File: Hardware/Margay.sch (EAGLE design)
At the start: 70 parts, among them IC1 ATMEGA644M, J1 CONN_42.54_SCREW, J2 CONN_6SCREW_2.54, Q1 FDN360P, Q2 DMG3404, Q3 2N7002, Q4 FDN360P, Q6 FDN360P, U2 FT231X-Q

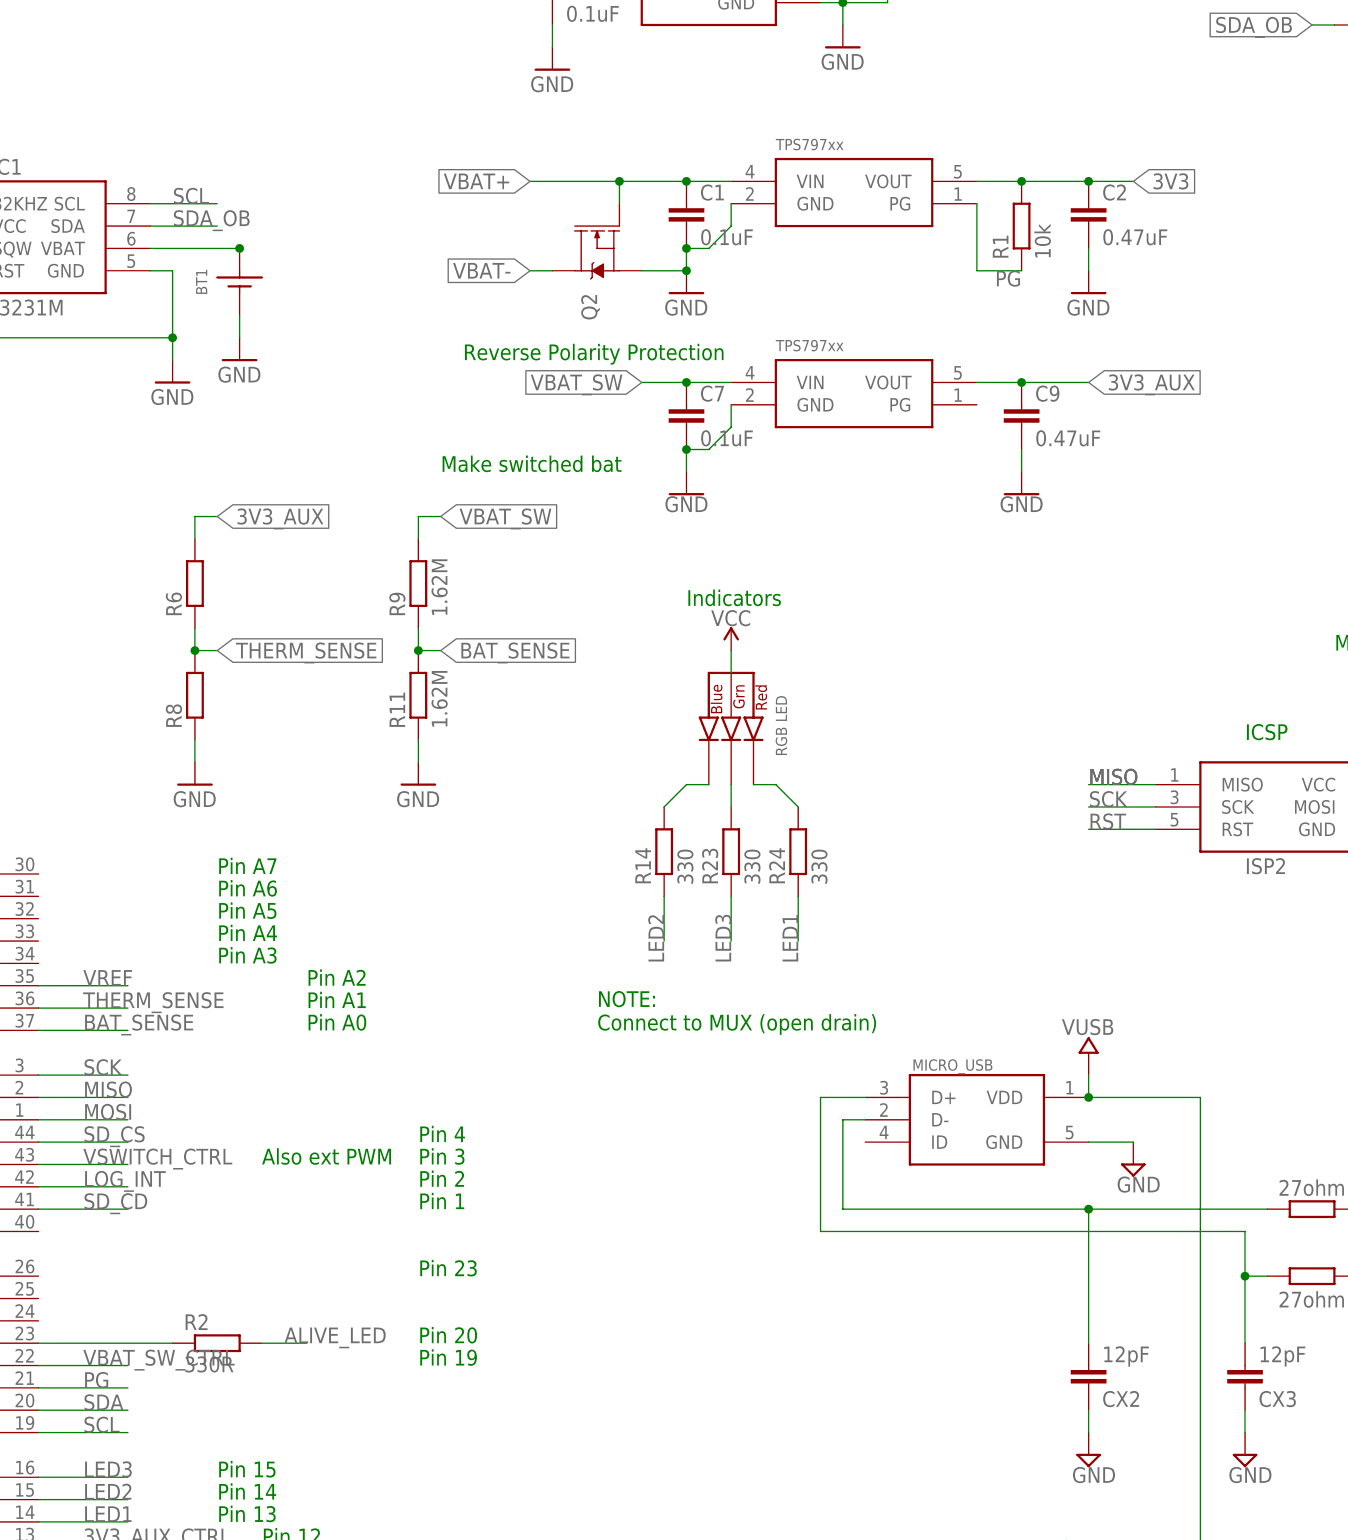
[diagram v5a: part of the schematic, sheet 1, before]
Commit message: Minor mod to hardware test, added BOM
Added independent BOM and did some clean up on the schematic
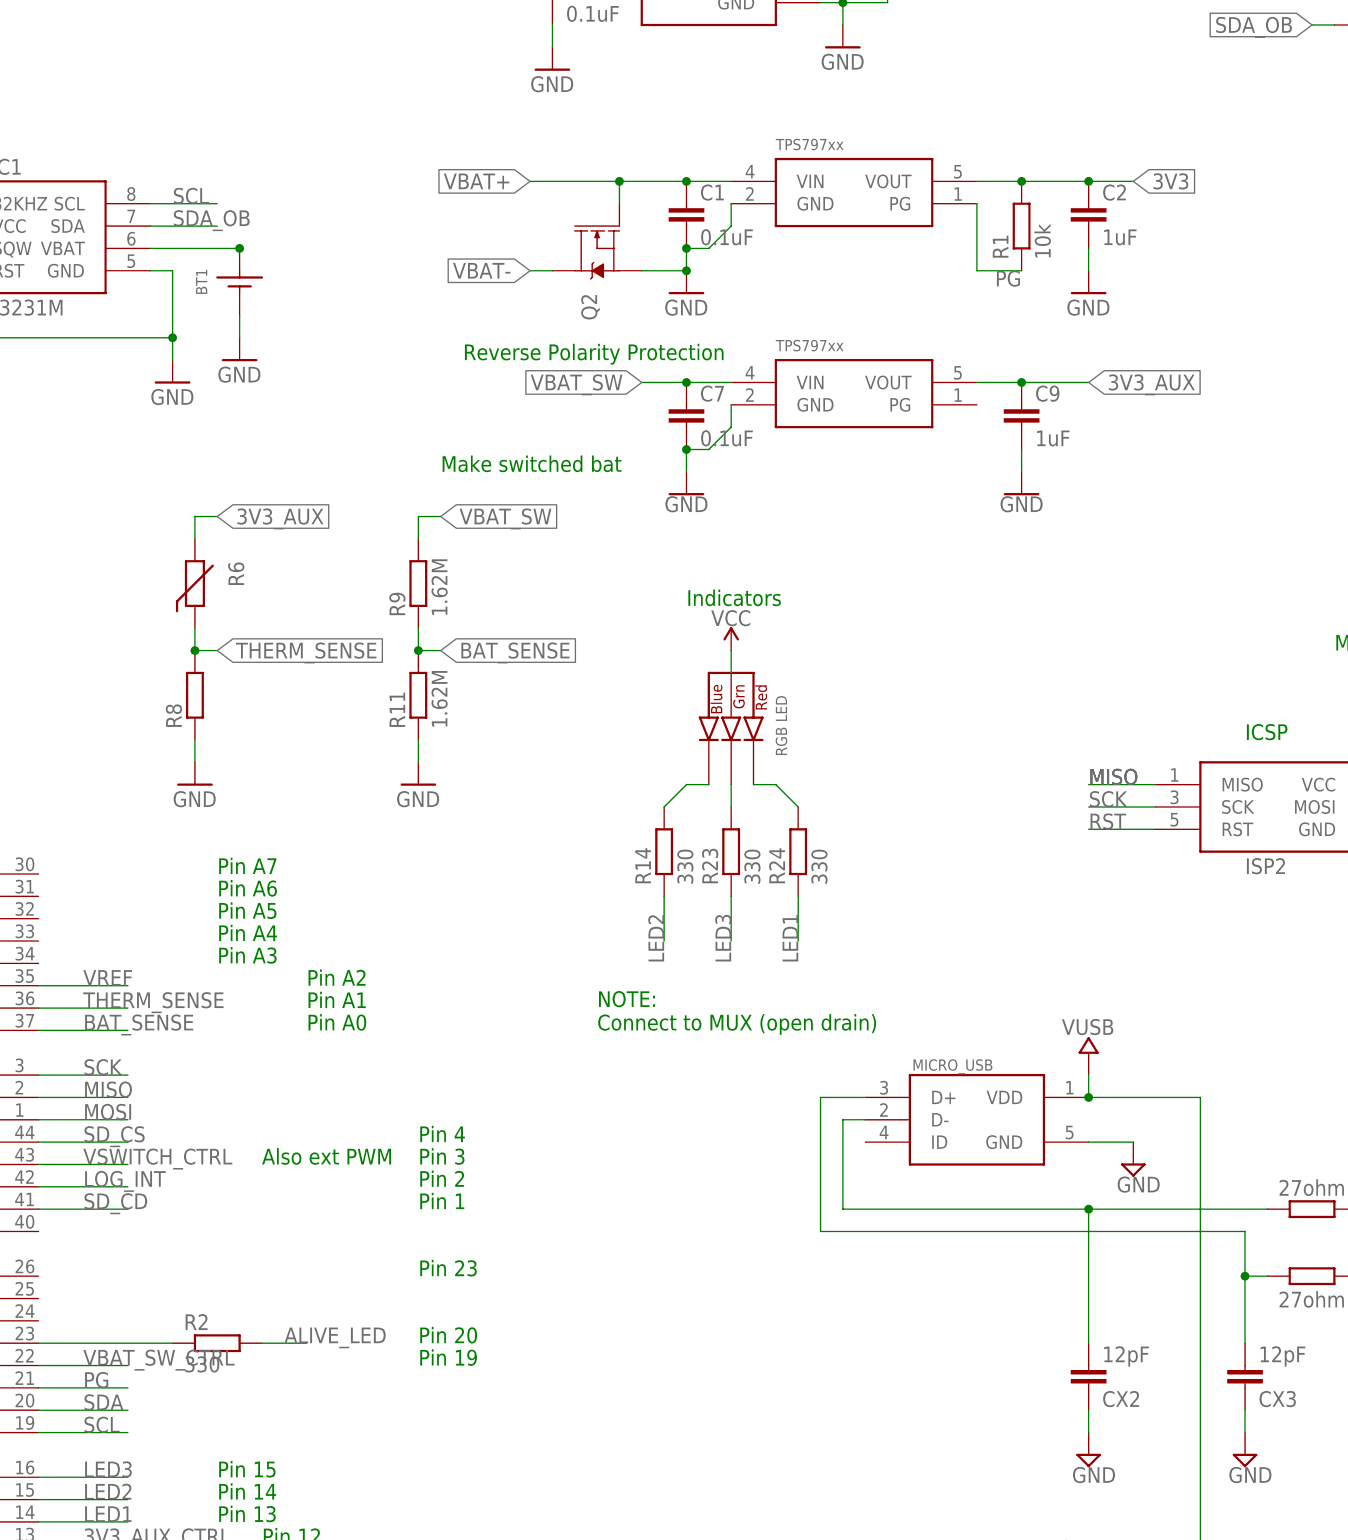
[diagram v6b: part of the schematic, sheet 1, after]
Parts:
- C1, C3, C4, C7: device bschulz_passives:C-EUC0603 -> bschulz_passives:C-EU0.1UFC0603
- C2, C9: value 0.47uF -> 1uF; device bschulz_passives:C-EUC0603 -> bschulz_passives:C-EU1UFC0603
- C25, C5: device bschulz:C-EU12PFC0603 -> bschulz_passives:C-EU12PFC0603
- C8: device bschulz:C-EUC0603 -> bschulz_passives:C-EU0.1UFC0603
- R1, R12, R15: device bschulz:R-EU_R0603 -> bschulz_passives:R-EU_10KR0603
- R11, R9: device bschulz:R-EU_R0603 -> bschulz_passives:R-EU_1.62MR0603
- R16: device bschulz_passives:R-EU_R0603 -> bschulz_passives:R-EU_180KR0603
- R17: device bschulz_passives:R-EU_R0603 -> bschulz_passives:R-EU_10KR0603
- R2: value 330R -> 330; device bschulz:R-EU_R0603 -> bschulz:R-EU_330R0603
- R6: device bschulz:R-EU_R0603 -> bschulz:THERMISTOR10K; DIGIKEY (none) -> 490-16279-1-ND; MF (none) -> Murata; MPN (none) -> NCU18XH103F60RB
- R8: DIGIKEY (none) -> P10KDBCT-ND; MF (none) -> Panasonic; MPN (none) -> ERA-3AEB103V
- U$3: device adafruit:SDMMC06132 -> bschulz:SDMMC06132
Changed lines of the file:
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@@
 <part name="U$9" library="bschulz" deviceset="BUTTON" device="4.2X3.2"/>
 <part name="GND20" library="SparkFun-PowerSymbols" deviceset="GND" device=""/>
-<part name="C25" library="bschulz" deviceset="C-EU" device="C0603" technology="12PF" value="12pF">
+<part name="C25" library="bschulz_passives" deviceset="C-EU" device="C0603" technology="12PF" value="12pF">
 <attribute name="DIGIKEY" value="1276-1254-1-ND"/>
 <attribute name="MF" value="Samsung"/>
@@
 </part>
 <part name="U$16" library="bschulz" deviceset="CLVBA-FKA" device=""/>
-<part name="C5" library="bschulz" deviceset="C-EU" device="C0603" technology="12PF" value="12pF">
+<part name="C5" library="bschulz_passives" deviceset="C-EU" device="C0603" technology="12PF" value="12pF">
 <attribute name="DIGIKEY" value="1276-1254-1-ND"/>
 <attribute name="MF" value="Samsung"/>
@@
 </part>
 <part name="C6" library="bschulz" deviceset="C-EU" device="C0603" technology="0.1UF" value="0.1uF"/>
-<part name="C8" library="bschulz" deviceset="C-EU" device="C0603" value="0.1uF"/>
+<part name="C8" library="bschulz_passives" deviceset="C-EU" device="C0603" technology="0.1UF" value="0.1uF"/>
 <part name="U$20" library="MyPOW" deviceset="VUSB" device=""/>
-<part name="U$3" library="adafruit" library_urn="urn:adsk.eagle:library:420" deviceset="SDMMC" device="06132"/>
+<part name="U$3" library="bschulz" deviceset="SDMMC" device="06132"/>
 <part name="Q1" library="bschulz" deviceset="MOSFET_PCH" device="-FDN360P" value="FDN360P"/>
 <part name="U$4" library="bschulz" deviceset="MIC842" device="" technology="H" value="MIC842H"/>
@@
 <part name="JP1" library="SparkFun-Jumpers" library_urn="urn:adsk.eagle:library:528" deviceset="JUMPER-SMT_3_1-NC_PASTE" device="_SILK" package3d_urn="urn:adsk.eagle:package:39293/1"/>
 <part name="U$6" library="bschulz" deviceset="TPS797*" device="" technology="33"/>
-<part name="C1" library="bschulz_passives" deviceset="C-EU" device="C0603" value="0.1uF"/>
+<part name="C1" library="bschulz_passives" deviceset="C-EU" device="C0603" technology="0.1UF" value="0.1uF"/>
 <part name="GND2" library="supply1" library_urn="urn:adsk.eagle:library:371" deviceset="GND" device=""/>
-<part name="C2" library="bschulz_passives" deviceset="C-EU" device="C0603" value="0.47uF"/>
+<part name="C2" library="bschulz_passives" deviceset="C-EU" device="C0603" technology="1UF" value="1uF"/>
 <part name="GND3" library="supply1" library_urn="urn:adsk.eagle:library:371" deviceset="GND" device=""/>
-<part name="R1" library="bschulz" deviceset="R-EU_" device="R0603" value="10k"/>
-<part name="R2" library="bschulz" deviceset="R-EU_" device="R0603" value="330R"/>
-<part name="R6" library="bschulz" deviceset="R-EU_" device="R0603"/>
-<part name="R8" library="bschulz" deviceset="R-EU_" device="R0603"/>
-<part name="R9" library="bschulz" deviceset="R-EU_" device="R0603" value="1.62M"/>
-<part name="R11" library="bschulz" deviceset="R-EU_" device="R0603" value="1.62M"/>
+<part name="R1" library="bschulz_passives" deviceset="R-EU_" device="R0603" technology="10K" value="10k"/>
+<part name="R2" library="bschulz" deviceset="R-EU_" device="R0603" technology="330" value="330"/>
+<part name="R6" library="bschulz" deviceset="THERMISTOR" device="" technology="10K">
+<attribute name="DIGIKEY" value="490-16279-1-ND"/>
+<attribute name="MF" value="Murata"/>
+<attribute name="MPN" value="NCU18XH103F60RB"/>
+</part>
+<part name="R8" library="bschulz" deviceset="R-EU_" device="R0603">
+<attribute name="DIGIKEY" value="P10KDBCT-ND "/>
+<attribute name="MF" value="Panasonic"/>
+<attribute name="MPN" value="ERA-3AEB103V"/>
+</part>
+<part name="R9" library="bschulz_passives" deviceset="R-EU_" device="R0603" technology="1.62M" value="1.62M"/>
+<part name="R11" library="bschulz_passives" deviceset="R-EU_" device="R0603" technology="1.62M" value="1.62M"/>
 <part name="GND4" library="supply1" library_urn="urn:adsk.eagle:library:371" deviceset="GND" device=""/>
 <part name="GND5" library="supply1" library_urn="urn:adsk.eagle:library:371" deviceset="GND" device=""/>
 <part name="U$7" library="bschulz" deviceset="MAX6070AAUT*" device="" technology="18"/>
-<part name="C3" library="bschulz_passives" deviceset="C-EU" device="C0603" value="0.1uF"/>
-<part name="C4" library="bschulz_passives" deviceset="C-EU" device="C0603" value="0.1uF"/>
+<part name="C3" library="bschulz_passives" deviceset="C-EU" device="C0603" technology="0.1UF" value="0.1uF"/>
+<part name="C4" library="bschulz_passives" deviceset="C-EU" device="C0603" technology="0.1UF" value="0.1uF"/>
 <part name="GND6" library="supply1" library_urn="urn:adsk.eagle:library:371" deviceset="GND" device=""/>
 <part name="U$8" library="bschulz" deviceset="MCP3425" device=""/>
@@
 <part name="J4" library="bschulz" deviceset="CONN_02" device="SCREW_2.54"/>
 <part name="J5" library="bschulz" deviceset="CONN_02" device="SCREW_2.54"/>
-<part name="R12" library="bschulz" deviceset="R-EU_" device="R0603" value="10k"/>
+<part name="R12" library="bschulz_passives" deviceset="R-EU_" device="R0603" technology="10K" value="10k"/>
 <part name="JP2" library="SparkFun-Jumpers" library_urn="urn:adsk.eagle:library:528" deviceset="JUMPER-SMT_2_NC_PASTE" device="_SILK" package3d_urn="urn:adsk.eagle:package:39282/1"/>
-<part name="R15" library="bschulz" deviceset="R-EU_" device="R0603" value="10k"/>
+<part name="R15" library="bschulz_passives" deviceset="R-EU_" device="R0603" technology="10K" value="10k"/>
 <part name="GND8" library="supply1" library_urn="urn:adsk.eagle:library:371" deviceset="GND" device=""/>
 <part name="Q2" library="bschulz" deviceset="MOSFET-NCH" device="-DMG3404L" value="DMG3404"/>
@@
 <part name="Q3" library="bschulz" deviceset="MOSFET-NCH" device="-2N7002PW" value="2N7002"/>
 <part name="Q4" library="bschulz" deviceset="MOSFET_PCH" device="-FDN360P" value="FDN360P"/>
-<part name="R16" library="bschulz_passives" deviceset="R-EU_" device="R0603" value="180k"/>
-<part name="R17" library="bschulz_passives" deviceset="R-EU_" device="R0603" value="10k"/>
+<part name="R16" library="bschulz_passives" deviceset="R-EU_" device="R0603" technology="180K" value="180k"/>
+<part name="R17" library="bschulz_passives" deviceset="R-EU_" device="R0603" technology="10K" value="10k"/>
 <part name="GND11" library="SparkFun-PowerSymbols" library_urn="urn:adsk.eagle:library:530" deviceset="GND" device=""/>
 <part name="U$10" library="bschulz" deviceset="TPS797*" device="" technology="33"/>
-<part name="C7" library="bschulz_passives" deviceset="C-EU" device="C0603" value="0.1uF"/>
-<part name="C9" library="bschulz_passives" deviceset="C-EU" device="C0603" value="0.47uF"/>
+<part name="C7" library="bschulz_passives" deviceset="C-EU" device="C0603" technology="0.1UF" value="0.1uF"/>
+<part name="C9" library="bschulz_passives" deviceset="C-EU" device="C0603" technology="1UF" value="1uF"/>
 <part name="GND12" library="SparkFun-PowerSymbols" library_urn="urn:adsk.eagle:library:530" deviceset="GND" device=""/>
 <part name="GND14" library="SparkFun-PowerSymbols" library_urn="urn:adsk.eagle:library:530" deviceset="GND" device=""/>
@@
 <attribute name="NAME" x="320.04" y="129.159" size="1.778" layer="95" font="vector" rot="R180"/>
 </instance>
-<instance part="U$6" gate="G$1" x="208.28" y="177.8"/>
+<instance part="U$6" gate="G$1" x="223.52" y="190.5"/>
 <instance part="C1" gate="G$1" x="205.74" y="187.96"/>
 <instance part="GND2" gate="1" x="205.74" y="177.8"/>
@@
 <instance part="R1" gate="G$1" x="243.84" y="185.42" rot="R90"/>
 <instance part="R2" gate="G$1" x="152.4" y="58.42"/>
-<instance part="R6" gate="G$1" x="149.86" y="144.78" rot="R90"/>
+<instance part="R6" gate="G$1" x="149.86" y="144.78" rot="R270"/>
 <instance part="R8" gate="G$1" x="149.86" y="132.08" rot="R90"/>
 <instance part="R9" gate="G$1" x="175.26" y="144.78" rot="R90"/>
@@
 <instance part="R17" gate="G$1" x="454.66" y="45.72" rot="R90"/>
 <instance part="GND11" gate="1" x="447.04" y="38.1"/>
-<instance part="U$10" gate="G$1" x="208.28" y="154.94"/>
+<instance part="U$10" gate="G$1" x="223.52" y="167.64"/>
 <instance part="C7" gate="G$1" x="205.74" y="165.1"/>
 <instance part="C9" gate="G$1" x="243.84" y="165.1"/>

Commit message: Added frames, major schematic clean up
Added frames and cleaned up and divided schematic into additional sheets
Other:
- note added: "Connectors, Indicators, Switching"
- note added: "Digital Core"
- note added: "Power"
- note added: "Sensor Peripherals"
